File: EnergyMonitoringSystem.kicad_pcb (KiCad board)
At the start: 6 copper layers, 170 x 115 mm, 188 parts, among them J201 USB_C_Receptacle_USB2.0_16P, J202 Screw_Terminal_01x02, J401 Conn_02x05_Counter_Clockwise, J402 Conn_02x05_Counter_Clockwise, J403 Conn_02x08_Counter_Clockwise, J501 Screw_Terminal_01x02, J502 Screw_Terminal_01x02, J503 Screw_Terminal_01x02, J504 Screw_Terminal_01x02, J505 Screw_Terminal_01x02, J506 Screw_Terminal_01x02, J601 DM3AT-SF-PEJM5_40_, J602 Screw_Terminal_01x03, Q201 STL6N3LLH6, SW401 SW_Push, SW402 SW_Push, U201 USBLC6-2P6, U202 STEF05SGR, U203 TCPP01-M12, U301 LDLN025M12R, U302 ST1PS02CQTR, U303 ST1PS02CQTR, U304 LM2664M6_NOPB, U401 STM32F103RGT6, U402 BLUENRG-M2SA, U501 ADS131M08IRSNR, U502 TSV911ILT, U503 TSV911ILT, U504 TSV911ILT, U601 EMIF06-MSD02N16, U602 ADM2565EBRNZ, Y401 16MHz, Y402 32.768KHz

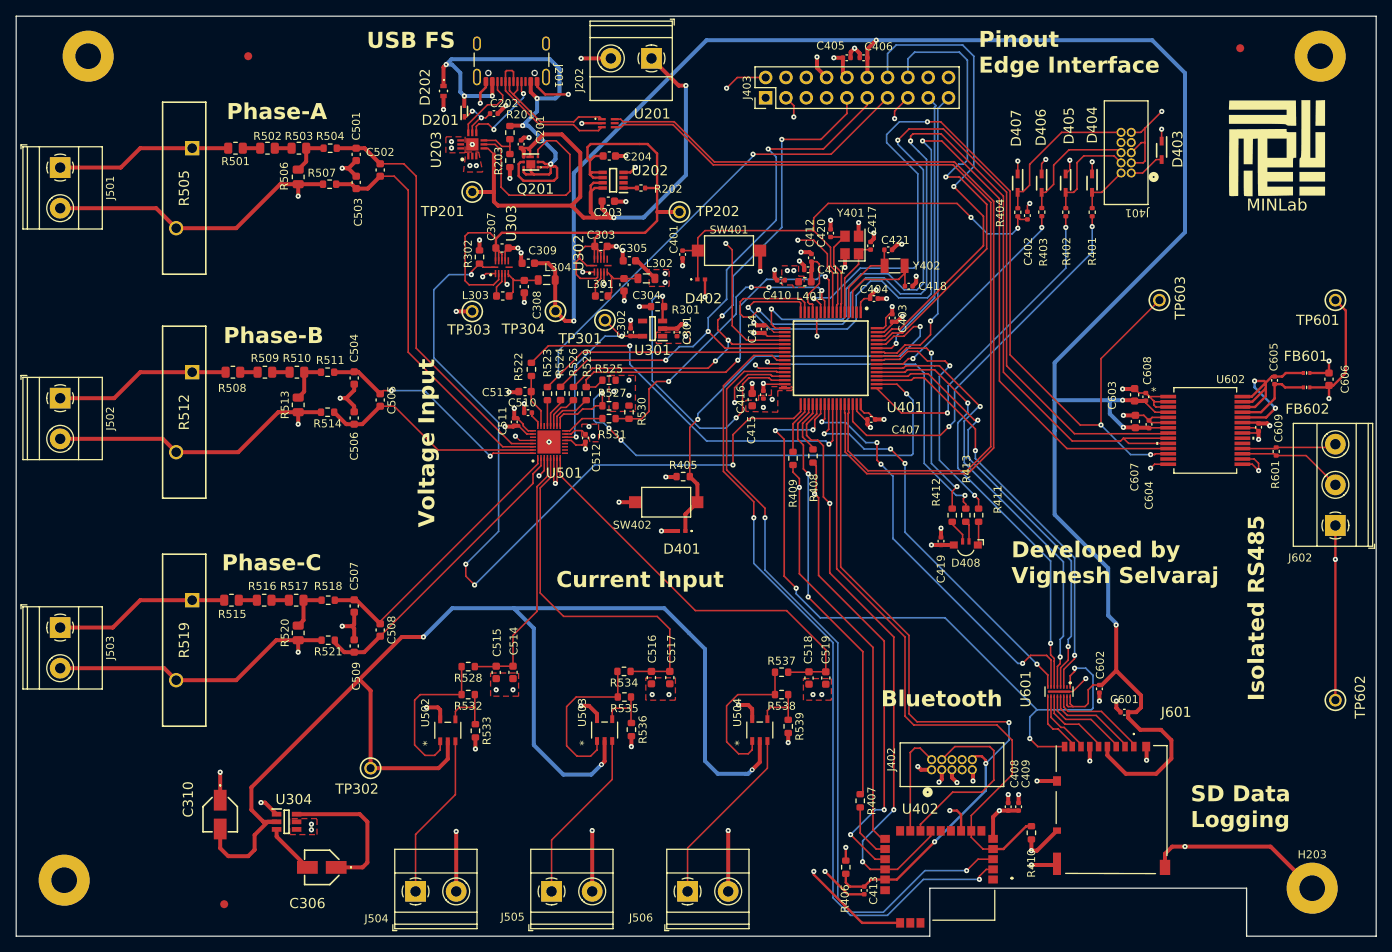
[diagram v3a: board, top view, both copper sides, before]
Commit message: updated mounting point and fiducial locations
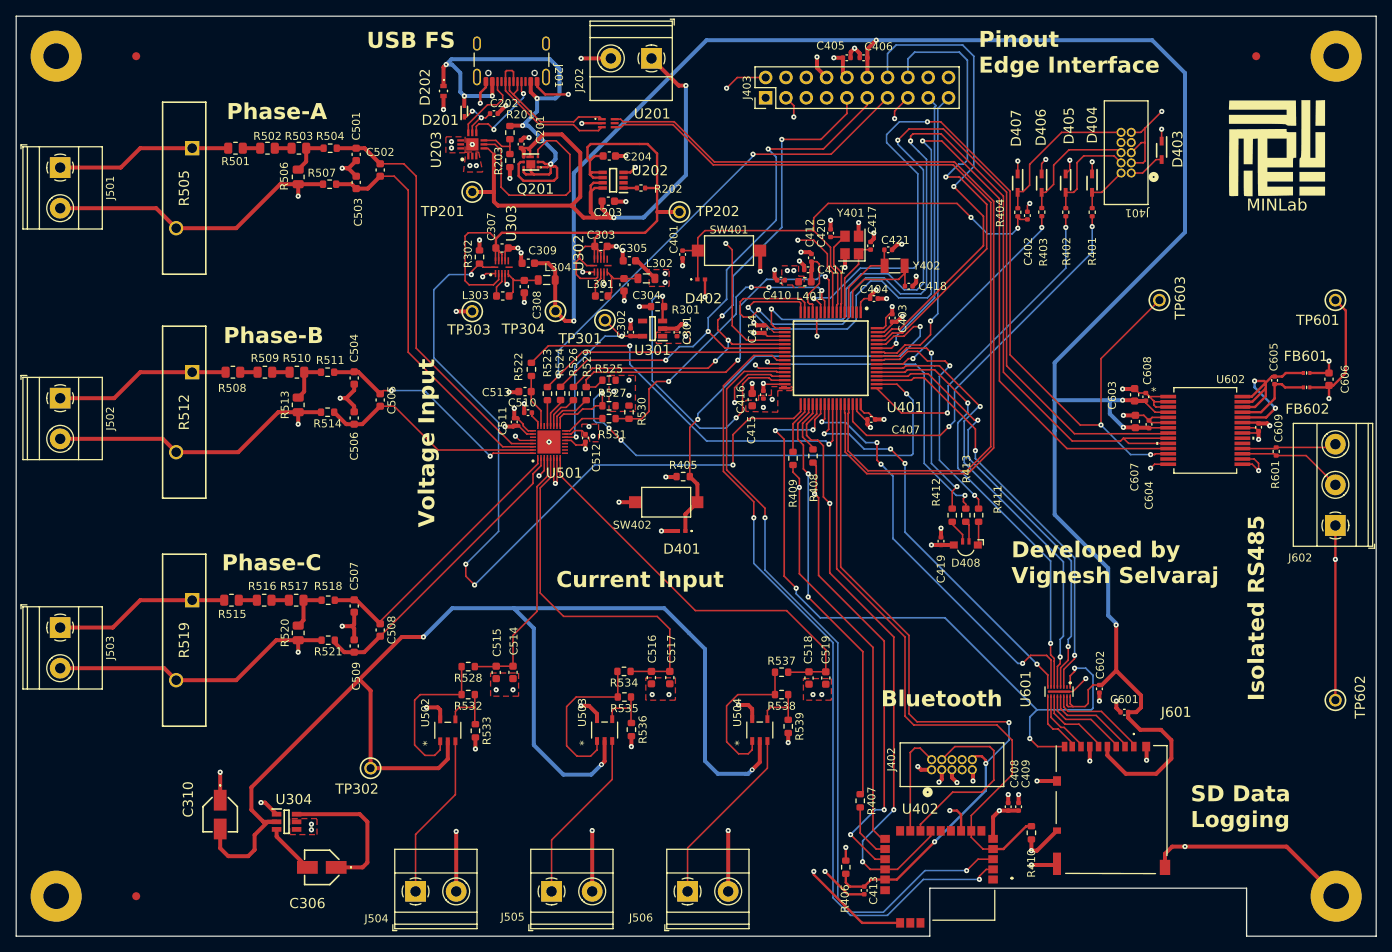
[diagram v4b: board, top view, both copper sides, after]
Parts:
- moved FM201 14.0 mm to (45.0, 43.0)
- moved FM203 11.0 mm to (45.0, 148.0)
- moved H201 4.00 mm to (35.0, 43.0)
- moved H203 3.16 mm to (195.0, 148.0)
- moved FM202 2.24 mm to (185.0, 43.0)
- moved H204 2.24 mm to (35.0, 148.0)
- moved H202 2.00 mm to (195.0, 43.0)
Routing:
- net GND: track 399.7 -> 403.1 mm
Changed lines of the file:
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@@
 		(pad_to_mask_clearance 0)
 		(allow_soldermask_bridges_in_footprints no)
+		(grid_origin 30 153)
 		(pcbplotparams
 			(layerselection 0x00010fc_ffffffff)
@@
 	(footprint "MountingHole:MountingHole_3.2mm_M3_Pad"
 		(layer "F.Cu")
-		(at 192 147)
+		(at 195 148)
 		(descr "Mounting Hole 3.2mm, M3")
 		(tags "mounting hole 3.2mm m3")
@@
 			(at 0 -4.2 0)
 			(layer "F.SilkS")
+			(hide yes)
 			(effects
 				(font
@@
 	(footprint "MountingHole:MountingHole_3.2mm_M3_Pad"
 		(layer "F.Cu")
-		(at 39 43)
+		(at 35 43)
 		(descr "Mounting Hole 3.2mm, M3")
 		(tags "mounting hole 3.2mm m3")
@@
 	(footprint "MountingHole:MountingHole_3.2mm_M3_Pad"
 		(layer "F.Cu")
-		(at 36 146)
+		(at 35 148)
 		(descr "Mounting Hole 3.2mm, M3")
 		(tags "mounting hole 3.2mm m3")
@@
 	(footprint "Fiducial:Fiducial_1mm_Mask2mm"
 		(layer "F.Cu")
-		(at 59 43)
+		(at 45 43)
 		(descr "Circular Fiducial, 1mm bare copper, 2mm soldermask opening (Level A)")
 		(tags "fiducial")
@@
 	(footprint "Fiducial:Fiducial_1mm_Mask2mm"
 		(layer "F.Cu")
-		(at 183 42)
+		(at 185 43)
 		(descr "Circular Fiducial, 1mm bare copper, 2mm soldermask opening (Level A)")
 		(tags "fiducial")
@@
 	(footprint "MountingHole:MountingHole_3.2mm_M3_Pad"
 		(layer "F.Cu")
-		(at 193 43)
+		(at 195 43)
 		(descr "Mounting Hole 3.2mm, M3")
 		(tags "mounting hole 3.2mm m3")
@@
 	(footprint "Fiducial:Fiducial_1mm_Mask2mm"
 		(layer "F.Cu")
-		(at 56 149)
+		(at 45 148)
 		(descr "Circular Fiducial, 1mm bare copper, 2mm soldermask opening (Level A)")
 		(tags "fiducial")
@@
 	)
 	(segment
-		(start 186.8 141.8)
-		(end 192 147)
-		(width 0.5)
-		(layer "F.Cu")
-		(net 2)
-	)
-	(segment
 		(start 85 139.9)
 		(end 85 147.4)
@@
 	)
 	(segment
-		(start 176.1 141.8)
-		(end 186.8 141.8)
-		(width 0.5)
-		(layer "F.Cu")
-		(net 2)
-	)
-	(segment
 		(start 35.5 119.5)
 		(end 48.5 119.5)
@@
 	)
 	(segment
+		(start 176.1 141.8)
+		(end 188.8 141.8)
+		(width 0.5)
+		(layer "F.Cu")
+		(net 2)
+	)
+	(segment
 		(start 92.924449 91.024449)
 		(end 92.4 90.5)
@@
 		(layer "F.Cu")
 		(net 2)
+	)
+	(segment
+		(start 188.8 141.8)
+		(end 195 148)
+		(width 0.5)
+		(layer "F.Cu")
+		(net 2)

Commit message: minor updates
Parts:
- added G***: LOGO, LOGO, F.Cu at (99.0, 104.0)
- added G***: Danger, LOGO, F.Cu at (69.0, 99.0)
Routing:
- net -DCDC_1: track 167.9 -> 171.2 mm
- net GND: track 403.1 -> 404.2 mm, vias 109 -> 116
- net /ADC/I_Phase_B_P: track 45.7 -> 44.6 mm
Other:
- board text added: "DANGER"
- board text added: "HOT SURFACE"
